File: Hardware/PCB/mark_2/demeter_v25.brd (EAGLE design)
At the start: 90 x 56 mm, 66 parts, among them IC1 4050, IC2 LM1117-5.0, IC3 LM1117-3.3, IC5 MCP3424, IC6 MCP23017SO, IC8 ATMEGA32U4-AU, Q1 IRLML6402, Q3 IRLML6402, Q5 IRLML6402

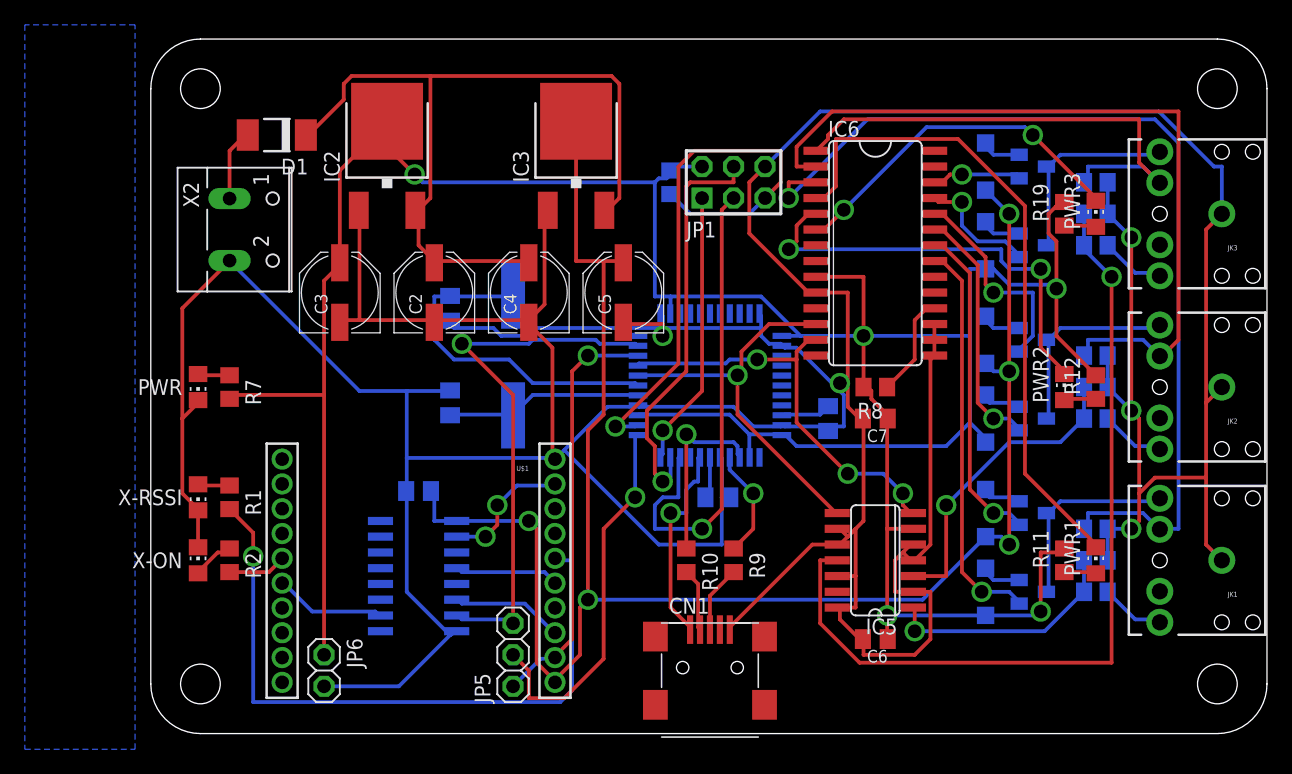
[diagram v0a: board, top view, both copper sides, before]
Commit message: 
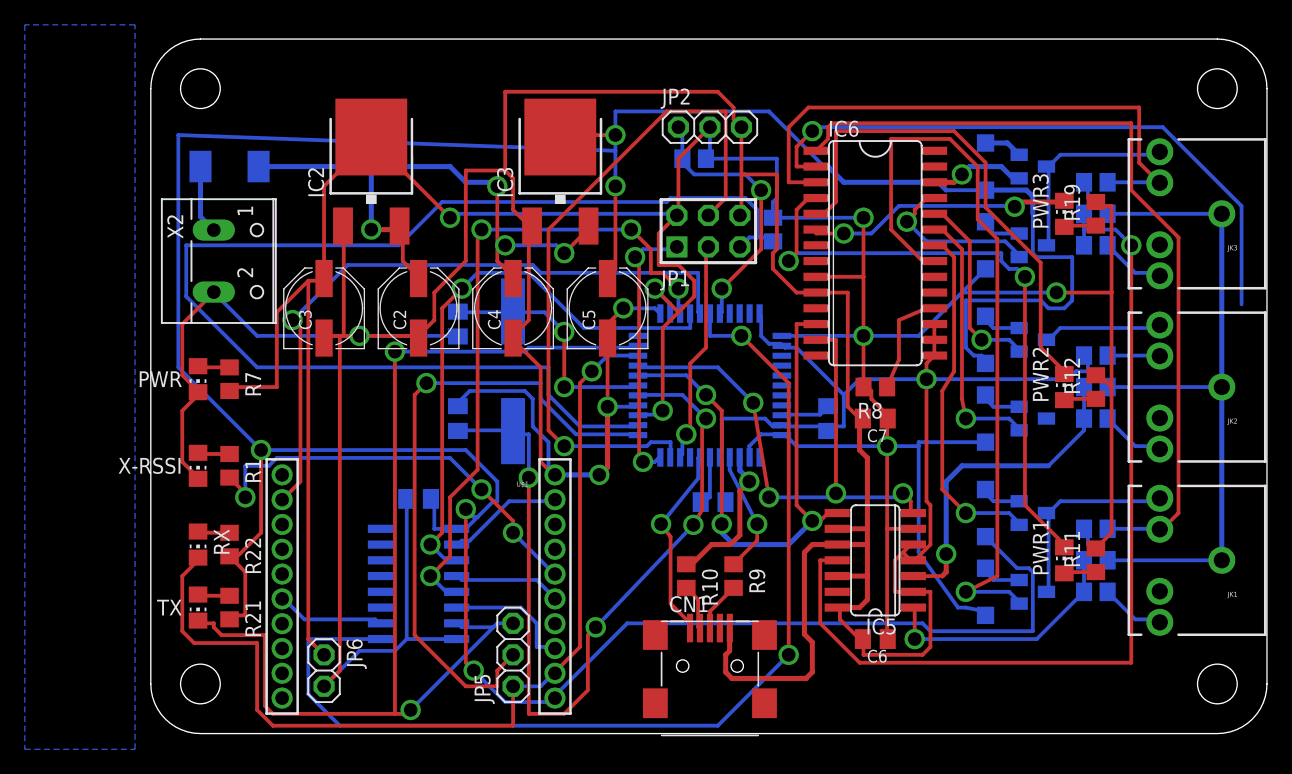
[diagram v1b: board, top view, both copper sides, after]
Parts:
- removed R2: (no value), mark_2:R0805
- removed X-ON: (no value), mark_2:CHIP-LED0805
- added JP2: (no value), mark_2:1X03
- added R20: 10k, mark_2:R0805
- added R21, R22: (no value), mark_2:R0805
- added RX, TX: (no value), mark_2:CHIP-LED0805
- moved R3 9.09 mm to (51.4, 41.9)
- moved D1 4.58 mm to (7.62, 47.0), flipped to the bottom, turned to 0 degrees
- moved JP1 4.43 mm to (46.2, 41.8)
- moved X2 2.84 mm to (7.62, 39.4)
- moved R1 2.54 mm to (7.62, 22.9)
- moved X-RSSI 2.54 mm to (5.08, 22.9)
- moved PWR1 2.54 mm to (74.9, 15.2)
- moved PWR3 2.54 mm to (74.9, 43.2)
- moved R11 2.54 mm to (77.5, 15.2)
- moved R19 2.54 mm to (77.5, 43.2)
- moved IC3 1.80 mm to (34.3, 47.0)
- moved C3 1.80 mm to (15.2, 35.6)
- moved C2 1.80 mm to (22.9, 35.6)
- moved C4 1.80 mm to (30.5, 35.6)
- moved IC2 1.80 mm to (19.1, 47.0)
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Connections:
- removed net CH4: IC5.13
- removed net N$10: R2.2, U$1.15
- removed net N$9: R2.1, X-ON.A
- new net DATA: IC8.29, JP2.1, R20.1
- new net N$36: R21.1, TX.A
- new net N$37: R22.1, RX.A
- new net RXLED: IC8.8
- new net TXLED: IC8.22
- net +3V3: now also R21.2, R22.2
- net +5V: now also JP2.2, R20.2
- net CTS: now also IC8.27
- net DTR: now also IC8.26
- net GND: now also JP2.3; no longer X-ON.C
- net RESET: now also IC8.25
- net RTS: now also IC8.28
- net RX: now also RX.C
- net SN1: now also IC6.1; no longer IC6.3
- net SN3: now also IC6.3; no longer IC6.1
- net TX: now also TX.C
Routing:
- net +3V3: track 142.7 -> 265.6 mm
- net RTS: track 0.00 -> 84.1 mm, vias 0 -> 2
- net CTS: track 0.00 -> 53.5 mm, vias 0 -> 1
- net RESET: track 0.00 -> 53.3 mm, vias 0 -> 4
- net RST: track 46.8 -> 99.7 mm, vias 1 -> 0
- net N$27: track 15.9 -> 66.1 mm, vias 0 -> 4
- net DTR: track 0.00 -> 46.3 mm, vias 0 -> 2
- net TX: track 43.6 -> 87.5 mm, vias 1 -> 2
- net RX: track 33.8 -> 76.2 mm
- net +5V: track 246.8 -> 282.9 mm, vias 5 -> 7
- net EN1-5: track 32.1 -> 61.0 mm
- net DATA: track 0.00 -> 22.0 mm, vias 0 -> 2
- net MOSI: track 33.5 -> 55.1 mm
- net EN: track 30.8 -> 51.7 mm
- net SCK: track 38.9 -> 18.1 mm
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
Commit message: 
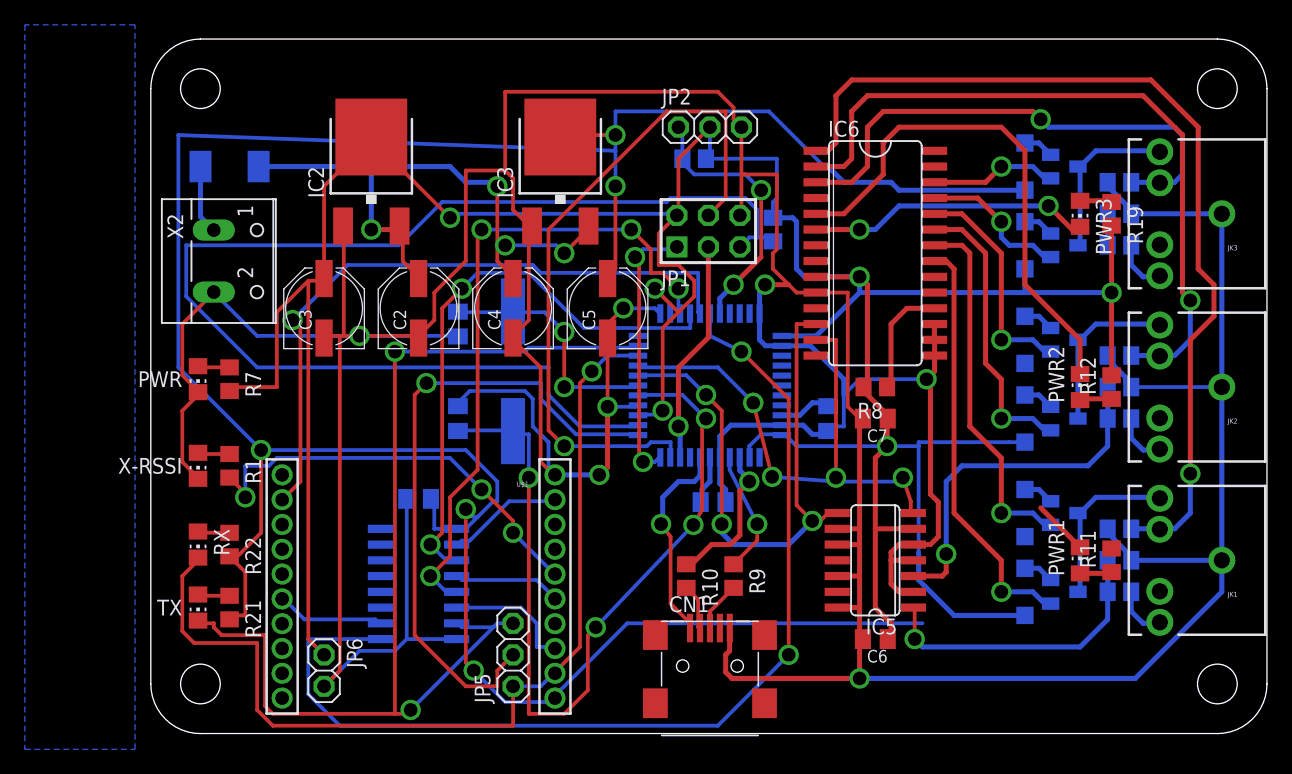
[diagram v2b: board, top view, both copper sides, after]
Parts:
- moved D2 3.17 mm to (71.8, 12.7)
- moved D3 3.17 mm to (71.8, 19.1)
- moved D4 3.17 mm to (71.8, 26.7)
- moved D5 3.17 mm to (71.8, 33.0)
- moved D6 3.17 mm to (71.8, 40.6)
- moved D7 3.17 mm to (71.8, 47.0)
- moved Q1 2.54 mm to (74.9, 12.7)
- moved Q2 2.54 mm to (74.9, 19.1)
- moved Q3 2.54 mm to (74.9, 26.7)
- moved Q4 2.54 mm to (74.9, 33.0)
- moved Q5 2.54 mm to (74.9, 40.6)
- moved Q6 2.54 mm to (74.9, 47.0)
- moved R13 1.91 mm to (79.4, 12.7)
- moved R14 1.91 mm to (79.4, 15.2)
- moved R15 1.91 mm to (79.4, 26.7)
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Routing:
- net CH3: track 73.4 -> 2.54 mm, vias 1 -> 0
- net +3V3: track 265.6 -> 219.3 mm
- net N$35: track 50.0 -> 4.49 mm, vias 2 -> 0
- net EN1-5: track 61.0 -> 33.8 mm
- net +5V: track 282.9 -> 272.3 mm, vias 7 -> 6
- net SN1: track 66.2 -> 74.7 mm, vias 0 -> 1
- net SN3: track 46.6 -> 42.2 mm, vias 0 -> 1
- net N$15: track 9.71 -> 14.0 mm
- net CH1: track 20.4 -> 24.2 mm
- net SN2: track 54.5 -> 57.6 mm
- net CH2: track 26.4 -> 29.0 mm
- net EN3-3: track 7.74 -> 10.3 mm
- net EN2-3: track 15.6 -> 18.1 mm
- net N$18: track 16.2 -> 13.7 mm
- net N$12: track 16.2 -> 13.7 mm
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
